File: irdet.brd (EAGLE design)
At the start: 50 x 45 mm, 66 parts, among them IC1 MEGA8-AI, IC2 78L05F, J1 PSH02-04WG, J2 PSH02-04WG, J3 PSH02-04WG, J4 PSH02-04WG, J5 22-05-7098-09, T1 BC847, T2 BC857, T3 BC847, T4 BC857, T5 BC847, T6 BC857, T7 BC847, T8 BC857, X1 MVE252-5-V, X2 MVE252-5-V

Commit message: Fix ERC issues.
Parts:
- RN2, RN4: value 10k -> 100k
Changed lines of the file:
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@@
 <layer number="14" name="Route14" color="22" fill="1" visible="no" active="no"/>
 <layer number="15" name="Route15" color="23" fill="1" visible="no" active="no"/>
-<layer number="16" name="Bottom" color="4" fill="1" visible="no" active="yes"/>
+<layer number="16" name="Bottom" color="4" fill="1" visible="yes" active="yes"/>
 <layer number="17" name="Pads" color="2" fill="1" visible="yes" active="yes"/>
 <layer number="18" name="Vias" color="2" fill="1" visible="yes" active="yes"/>
-<layer number="19" name="Unrouted" color="6" fill="1" visible="no" active="yes"/>
+<layer number="19" name="Unrouted" color="6" fill="1" visible="yes" active="yes"/>
 <layer number="20" name="Dimension" color="24" fill="1" visible="yes" active="yes"/>
 <layer number="21" name="tPlace" color="7" fill="1" visible="yes" active="yes"/>
-<layer number="22" name="bPlace" color="7" fill="1" visible="no" active="yes"/>
-<layer number="23" name="tOrigins" color="15" fill="1" visible="no" active="yes"/>
-<layer number="24" name="bOrigins" color="15" fill="1" visible="no" active="yes"/>
-<layer number="25" name="tNames" color="7" fill="1" visible="yes" active="yes"/>
+<layer number="22" name="bPlace" color="7" fill="1" visible="yes" active="yes"/>
+<layer number="23" name="tOrigins" color="15" fill="1" visible="yes" active="yes"/>
+<layer number="24" name="bOrigins" color="15" fill="1" visible="yes" active="yes"/>
+<layer number="25" name="tNames" color="7" fill="1" visible="no" active="yes"/>
 <layer number="26" name="bNames" color="7" fill="1" visible="no" active="yes"/>
 <layer number="27" name="tValues" color="7" fill="1" visible="no" active="yes"/>
@@
 <layer number="44" name="Drills" color="7" fill="1" visible="no" active="yes"/>
 <layer number="45" name="Holes" color="7" fill="1" visible="no" active="yes"/>
-<layer number="46" name="Milling" color="3" fill="1" visible="no" active="yes"/>
+<layer number="46" name="Milling" color="3" fill="1" visible="yes" active="yes"/>
 <layer number="47" name="Measures" color="7" fill="1" visible="no" active="yes"/>
 <layer number="48" name="Document" color="7" fill="1" visible="no" active="yes"/>
-<layer number="49" name="Reference" color="7" fill="1" visible="no" active="yes"/>
+<layer number="49" name="Reference" color="7" fill="1" visible="yes" active="yes"/>
 <layer number="50" name="dxf" color="7" fill="1" visible="no" active="no"/>
 <layer number="51" name="tDocu" color="7" fill="1" visible="yes" active="yes"/>
-<layer number="52" name="bDocu" color="7" fill="1" visible="no" active="yes"/>
+<layer number="52" name="bDocu" color="7" fill="1" visible="yes" active="yes"/>
 <layer number="53" name="tGND_GNDA" color="7" fill="9" visible="no" active="no"/>
 <layer number="54" name="bGND_GNDA" color="1" fill="9" visible="no" active="no"/>
@@
 <attribute name="VALUE" x="11.557" y="38.989" size="1.016" layer="28" rot="MR180"/>
 </element>
-<element name="RN2" library="resistor-net" library_urn="urn:adsk.eagle:library:343" package="CTS742C083" package3d_urn="urn:adsk.eagle:package:24985/1" value="10k" x="12.7" y="33.655" smashed="yes" rot="MR0">
-<attribute name="LCSC_PART" value="C29718" x="12.7" y="33.655" size="1.778" layer="28" rot="MR0" display="off"/>
+<element name="RN2" library="resistor-net" library_urn="urn:adsk.eagle:library:343" package="CTS742C083" package3d_urn="urn:adsk.eagle:package:24985/1" value="100k" x="12.7" y="33.655" smashed="yes" rot="MR0">
+<attribute name="LCSC_PART" value="C173315" x="12.7" y="33.655" size="1.778" layer="28" rot="MR0" display="off"/>
 <attribute name="MF" value="" x="-33.02" y="-14.605" size="1.778" layer="28" rot="MR0" display="off"/>
 <attribute name="MPN" value="" x="-33.02" y="-14.605" size="1.778" layer="28" rot="MR0" display="off"/>
@@
 <attribute name="VALUE" x="36.322" y="38.989" size="1.016" layer="28" rot="MR180"/>
 </element>
-<element name="RN4" library="resistor-net" library_urn="urn:adsk.eagle:library:343" package="CTS742C083" package3d_urn="urn:adsk.eagle:package:24985/1" value="10k" x="37.465" y="33.655" smashed="yes" rot="MR0">
-<attribute name="LCSC_PART" value="C29718" x="37.465" y="33.655" size="1.778" layer="28" rot="MR0" display="off"/>
+<element name="RN4" library="resistor-net" library_urn="urn:adsk.eagle:library:343" package="CTS742C083" package3d_urn="urn:adsk.eagle:package:24985/1" value="100k" x="37.465" y="33.655" smashed="yes" rot="MR0">
+<attribute name="LCSC_PART" value="C173315" x="37.465" y="33.655" size="1.778" layer="28" rot="MR0" display="off"/>
 <attribute name="MF" value="" x="-18.415" y="-14.605" size="1.778" layer="28" rot="MR0" display="off"/>
 <attribute name="MPN" value="" x="-18.415" y="-14.605" size="1.778" layer="28" rot="MR0" display="off"/>

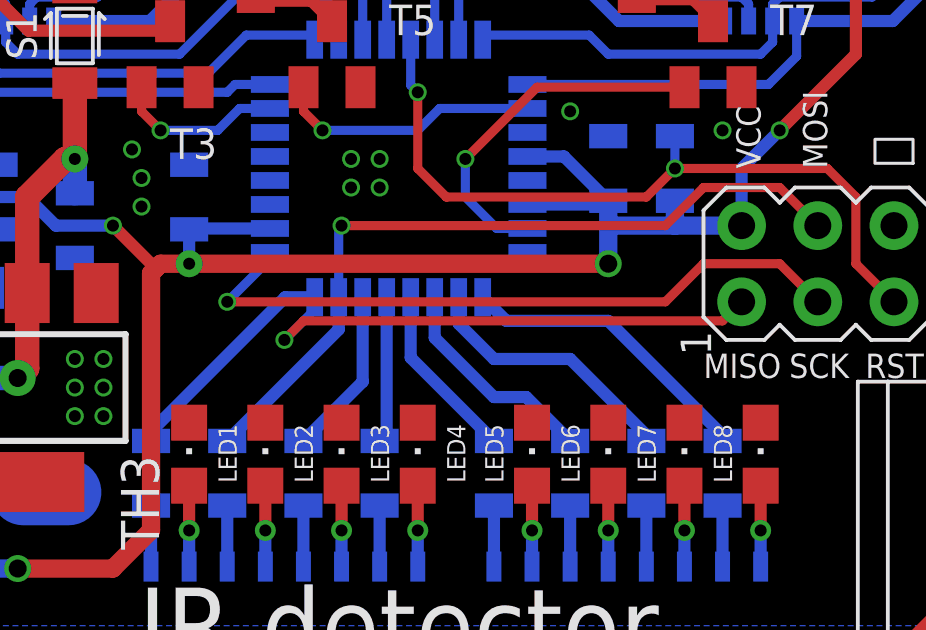
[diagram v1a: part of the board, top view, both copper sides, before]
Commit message: Add status LED.
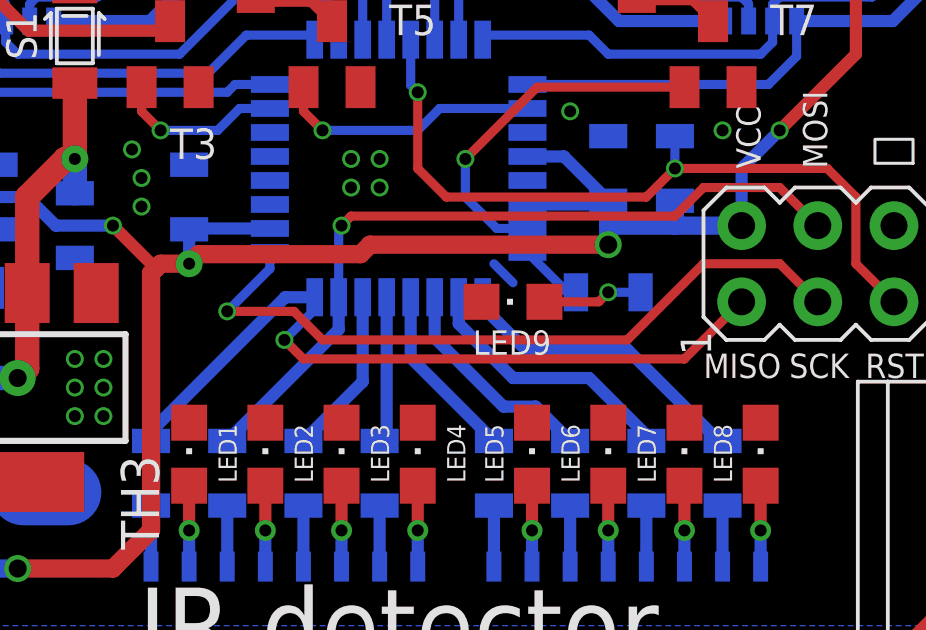
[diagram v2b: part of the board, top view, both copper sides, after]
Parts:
- added LED9: RED, led:CHIPLED_0805
- added R15: 1k, rcl:R0805
- LED1, LED2, LED3, LED4, LED5, LED6, LED7, LED8: value (none) -> YEL
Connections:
- new net N$34: IC1.8, R15.2
- new net N$47: LED9.A, R15.1
- net GND: now also LED9.C
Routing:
- net N$47: track 0.00 -> 3.33 mm, vias 0 -> 1
- net N$34: track 0.00 -> 2.17 mm
- net SCK: track 23.0 -> 24.2 mm
- net GND: track 0.00 -> 0.90 mm
- net MISO/OUT1: track 25.2 -> 25.8 mm

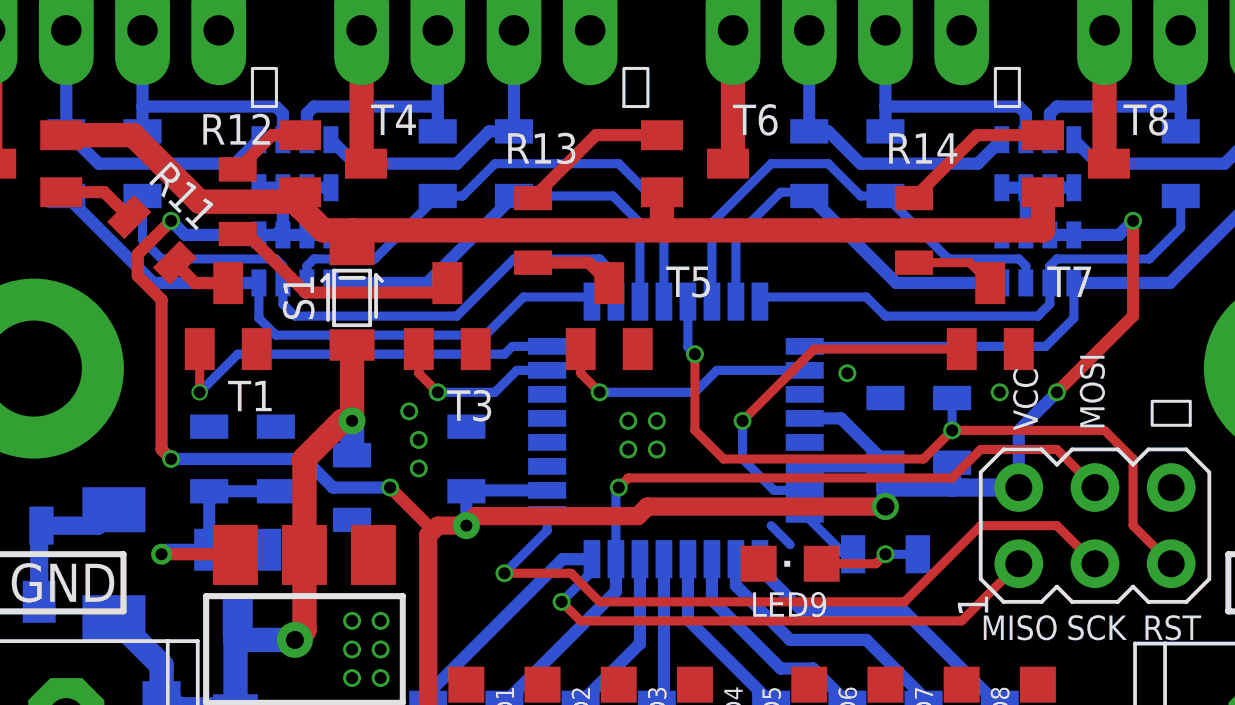
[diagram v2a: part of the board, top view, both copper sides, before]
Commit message: Add resistors to transistor's base.
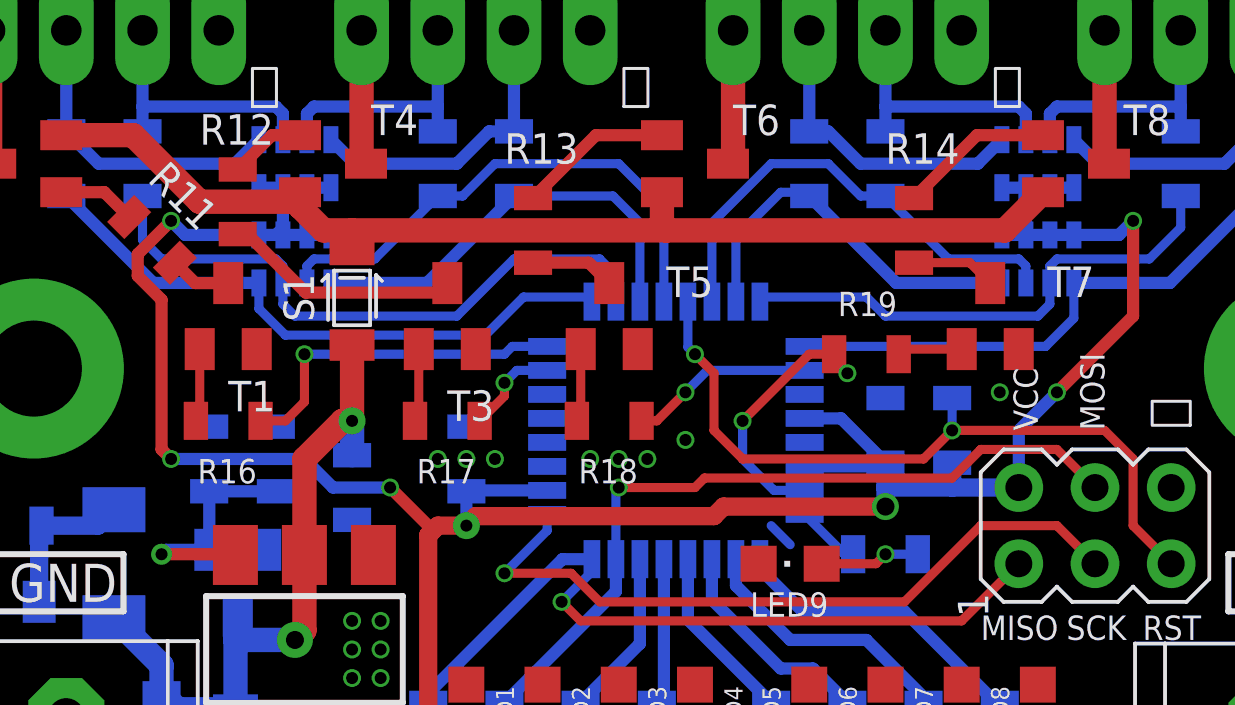
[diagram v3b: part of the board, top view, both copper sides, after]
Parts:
- added R16, R17, R18, R19: 1k, rcl:R0805
- R11, R12, R13, R14: value 4k7 -> 1k
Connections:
- new net N$48: R17.2, T3.B
- new net N$49: R16.2, T1.B
- new net N$50: R18.2, T5.B
- new net N$51: R19.2, T7.B
- net CPUPOW1-2: now also R16.1; no longer T1.B
- net CPUPOW3-4: now also R17.1; no longer T3.B
- net CPUPOW5-6: now also R18.1; no longer T5.B
- net CPUPOW7-8: now also R19.1; no longer T7.B
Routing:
- net CPUPOW7-8: track 12.1 -> 7.75 mm
- net CPUPOW5-6: track 8.84 -> 6.14 mm
- net N$49: track 0.00 -> 2.45 mm
- net N$50: track 0.00 -> 2.45 mm
- net N$48: track 0.00 -> 2.45 mm
- net CPUPOW3-4: track 5.65 -> 3.21 mm
- net N$51: track 0.00 -> 2.17 mm
- net CPUPOW1-2: track 13.7 -> 11.5 mm
- net N$42: track 37.8 -> 37.1 mm

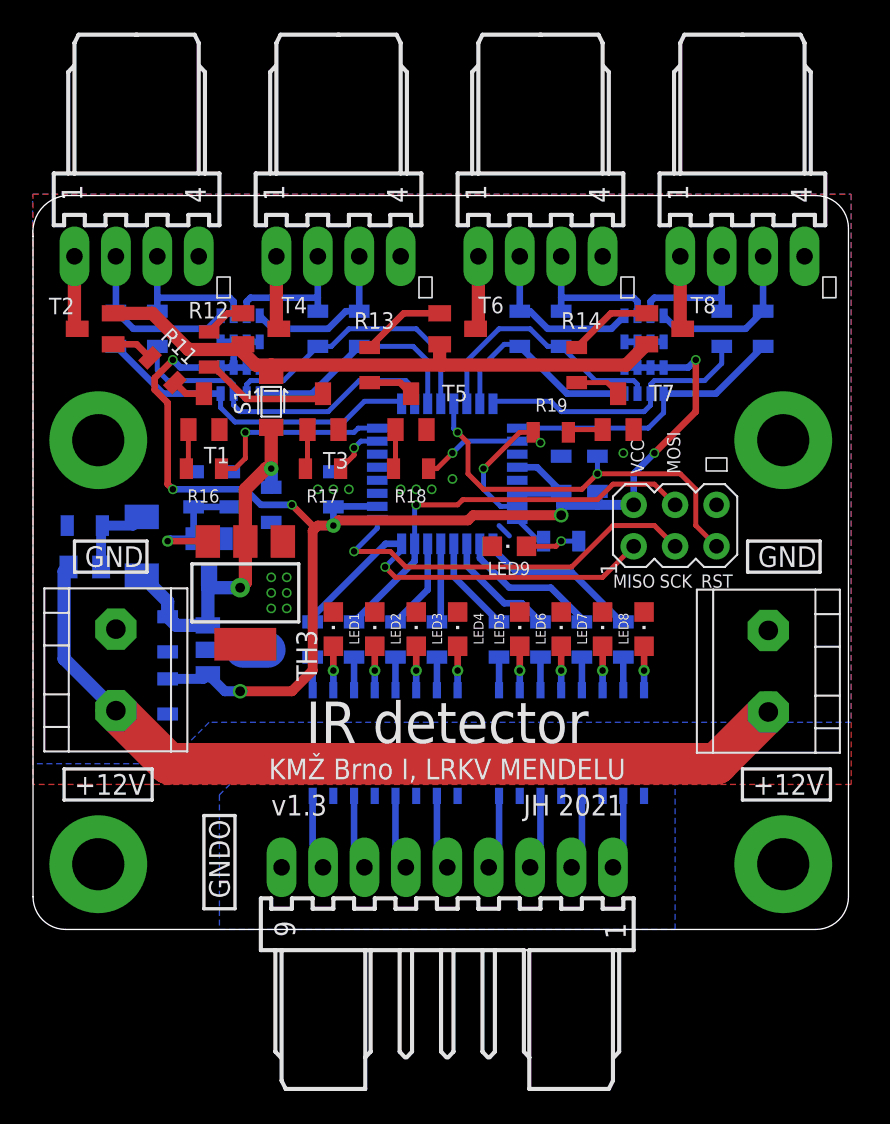
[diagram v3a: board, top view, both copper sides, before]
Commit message: Update IR diode power.
* Add stabilizer to 8V + big resistor for current ~200 mA.
* Remove overvoltage protection.
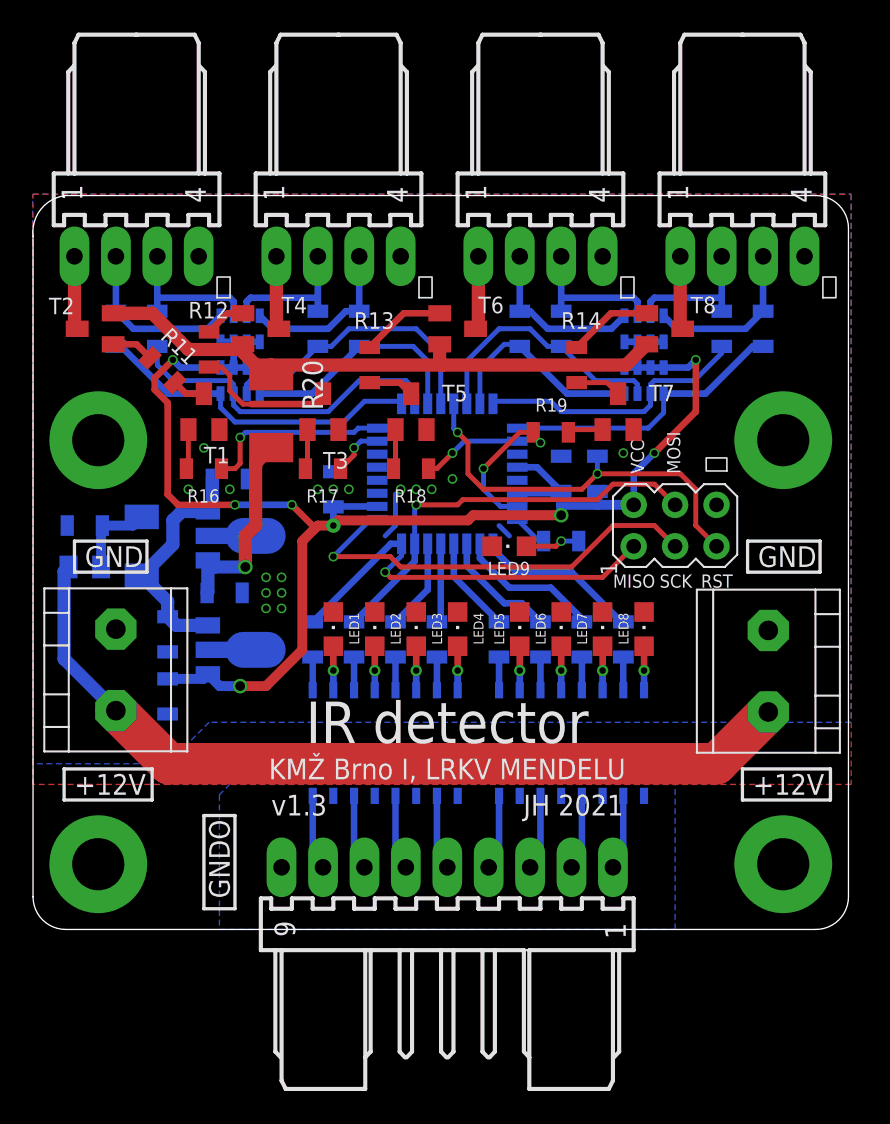
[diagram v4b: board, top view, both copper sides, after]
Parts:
- removed C13: 100n, rcl:C0805
- removed D2: BZX84C18, diode:SOT23
- removed R2: 2k2, rcl:R0805
- removed S1: AL5809-100, current-stabilizers:POWERDI-123
- removed TH3: BT148, ElectroKrt:SOT223
- added C3: 22u, rcl:C0805
- added IC3: 78L08F, linear:SOT89
- added R20: 68R, rcl:R2010
- F1: value 200mA -> 400mA
- moved C16 3.00 mm to (12.1, 27.6), turned to 180 degrees
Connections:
- removed net N$57: C13.1, D2.1, R2.2, TH3.3
- new net +8V: C3.1, IC3.1, R20.2
- net +12V: now also IC3.3; no longer D2.3, S1.IN, TH3.2
- net GND: now also C3.2, IC3.2, IC3.2@1; no longer C13.2, R2.1, TH3.1
- net N$42: now also R20.1; no longer S1.OUT
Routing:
- net +8V: track 0.00 -> 12.5 mm, vias 0 -> 1
- net +12V: track 22.9 -> 14.5 mm, vias 2 -> 0
- net N$57: track 8.30 -> 0.00 mm, vias 1 -> 0
- net GND: track 0.90 -> 4.15 mm, vias 15 -> 18
- net SCK: track 24.2 -> 26.4 mm
- net +5V: track 98.0 -> 97.0 mm
- net N$37: track 7.92 -> 8.75 mm

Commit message: Minor tweaks.
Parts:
- moved C5 1.27 mm to (6.35, 36.8)
- moved C4 0.95 mm to (8.57, 36.8)
- moved R17 0.32 mm to (18.1, 28.3)
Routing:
- net IN1: track 20.5 -> 19.4 mm
- net IN2: track 20.7 -> 20.0 mm
- net N$1: track 10.6 -> 9.82 mm
- net N$2: track 9.02 -> 8.46 mm
- net GND: vias 18 -> 23

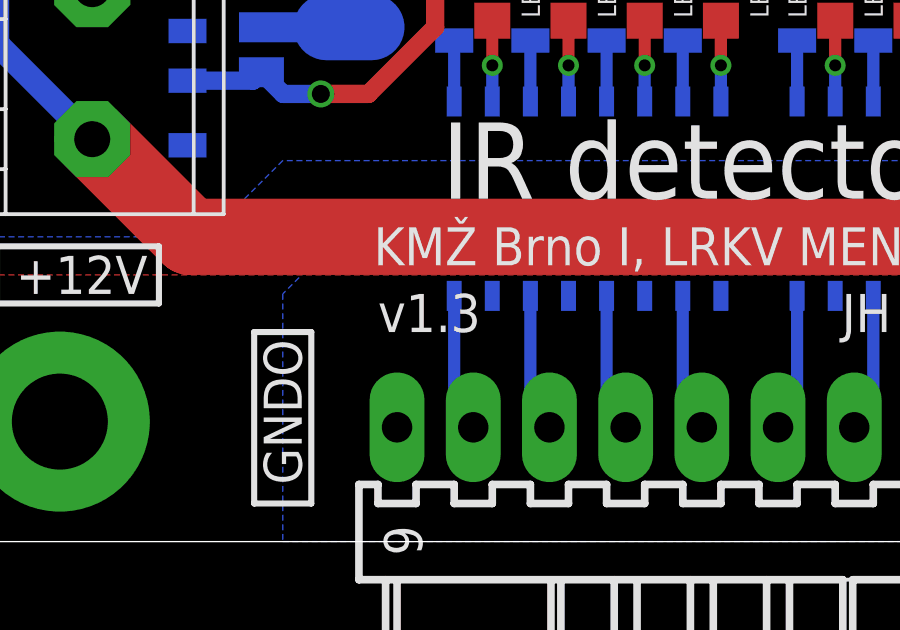
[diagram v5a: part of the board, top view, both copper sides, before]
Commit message: Change version to 2.0.
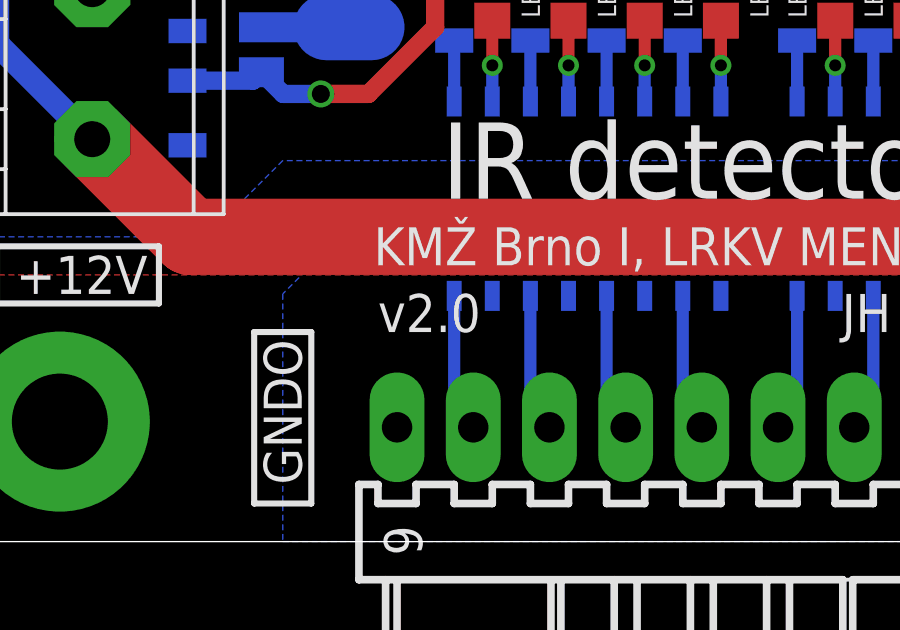
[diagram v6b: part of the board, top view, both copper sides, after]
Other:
- board text added: "v2.0"
- board text removed: "v1.3"
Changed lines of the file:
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@@
 <text x="25.4" y="9.2075" size="1.27" layer="25" align="bottom-center">KMŽ Brno I, LRKV MENDELU</text>
 <text x="36.195" y="6.985" size="1.27" layer="25" align="bottom-right">JH 2021</text>
-<text x="14.605" y="6.985" size="1.27" layer="25">v1.3</text>
+<text x="14.605" y="6.985" size="1.27" layer="25">v2.0</text>
 <text x="42.545" y="27.94" size="1.27" layer="25" rot="R90">⏚</text>
 <text x="37.465" y="27.94" size="0.8128" layer="25" rot="R90">VCC</text>
